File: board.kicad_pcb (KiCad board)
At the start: 2 copper layers, 32.9 x 46.8 mm, 20 parts, among them P1 CONN_8, P2 CONN_8, U1 74LS595, U2 74LS595, U3 CD74ACT257M96, U4 CD74ACT257M96, U5 74LVC1G14, U6 FDC6305N, U7 RG7SEG

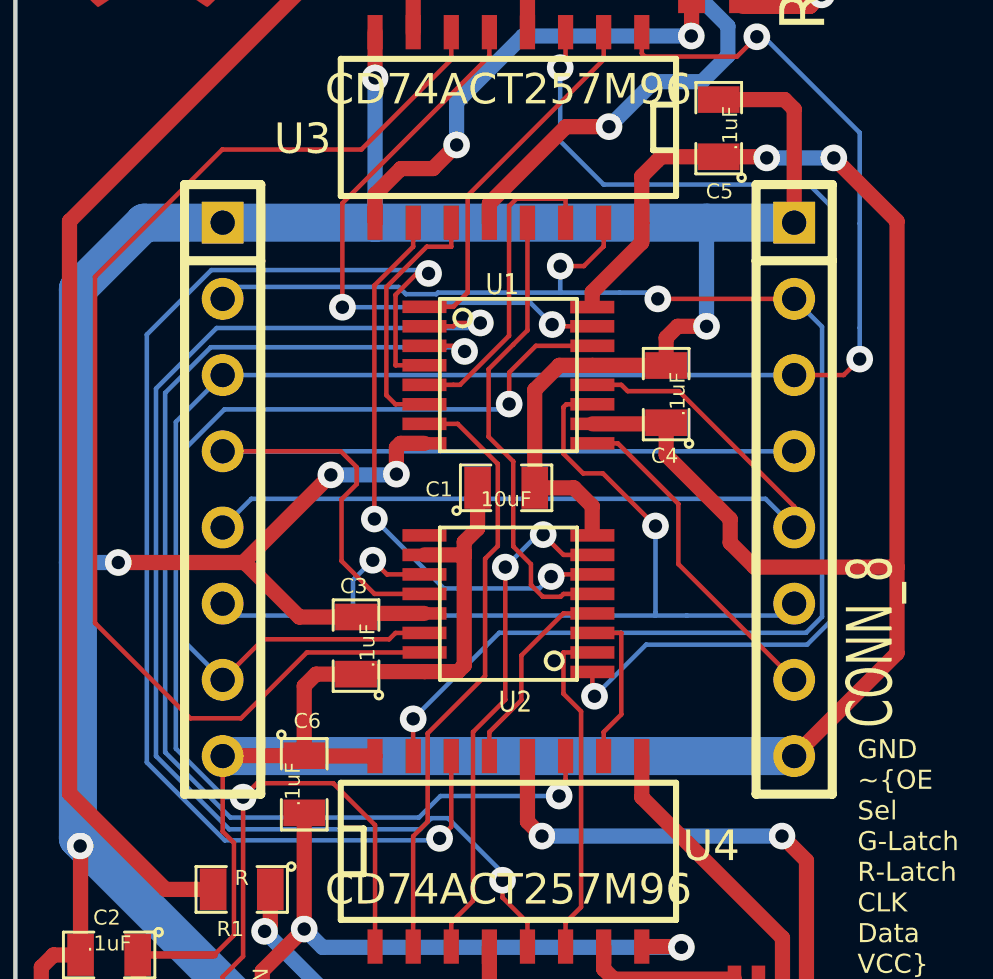
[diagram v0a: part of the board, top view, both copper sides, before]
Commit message: Update board layout and gerber outputs
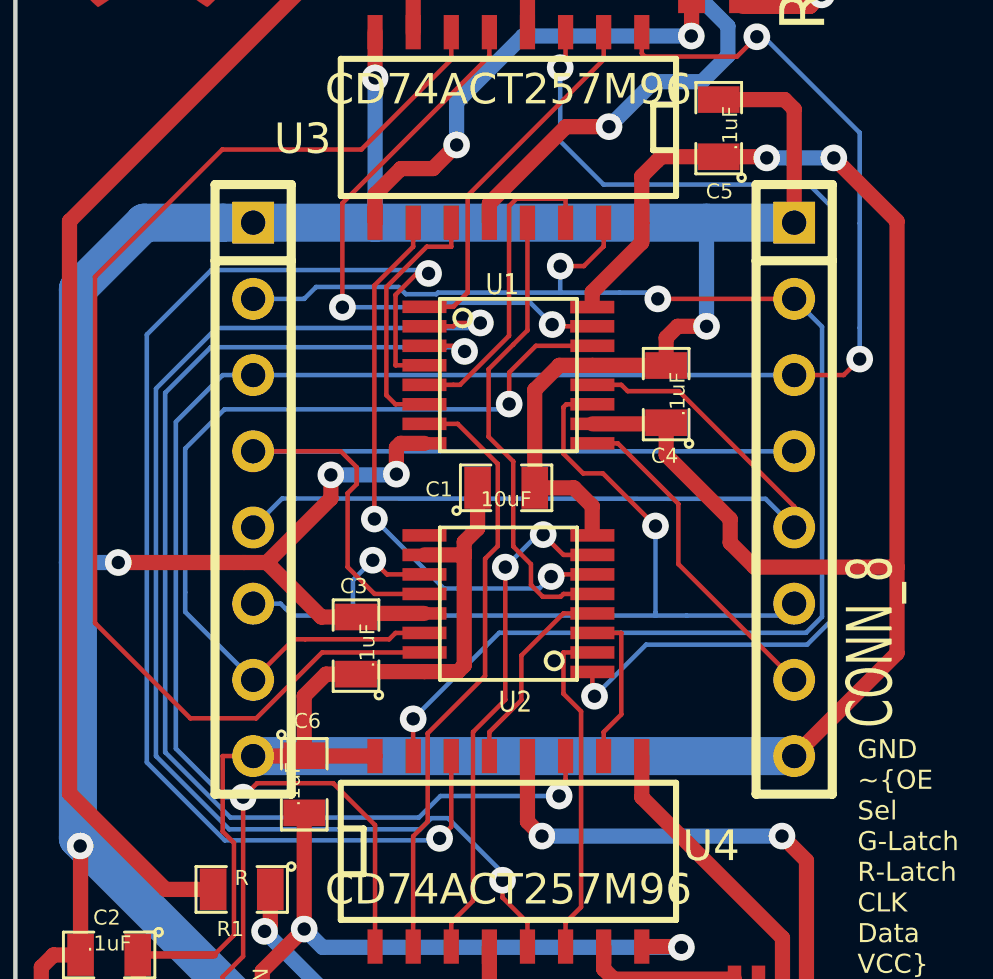
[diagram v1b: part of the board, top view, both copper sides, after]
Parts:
- moved P1 1.02 mm to (118.5, 127.0)
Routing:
- net VCC: track 100.5 -> 98.1 mm
- net /Glatch: track 30.3 -> 28.2 mm
- net /OE: track 50.4 -> 49.4 mm
- net /Clk: track 33.0 -> 32.0 mm
- net /Rlatch: track 28.9 -> 27.9 mm
- net /Din: track 31.2 -> 30.6 mm
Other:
- net class Default: trace_width 0.254 -> 0.1524
